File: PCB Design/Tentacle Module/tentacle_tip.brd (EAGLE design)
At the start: 45.7 x 15.2 mm, 8 parts, among them U2 ADXL345PATRICK

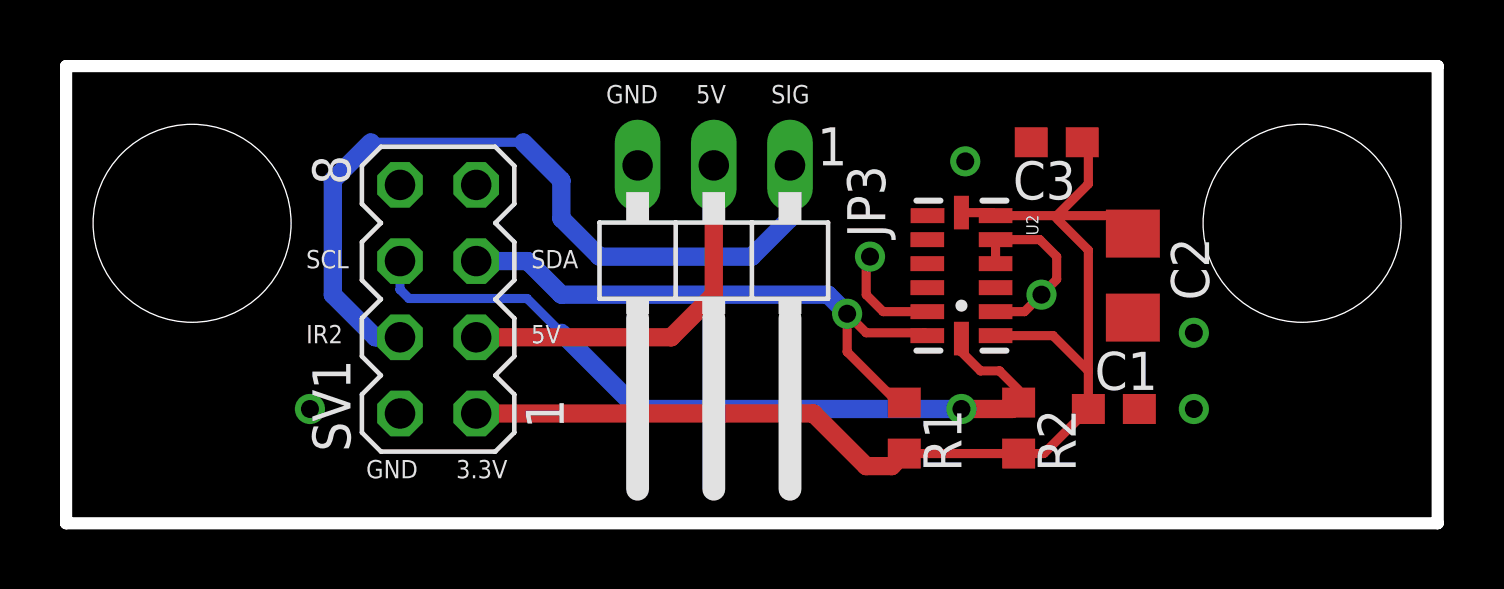
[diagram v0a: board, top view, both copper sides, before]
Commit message: Fixed up the  Tentacle tip board
routed the airwires that I forgot
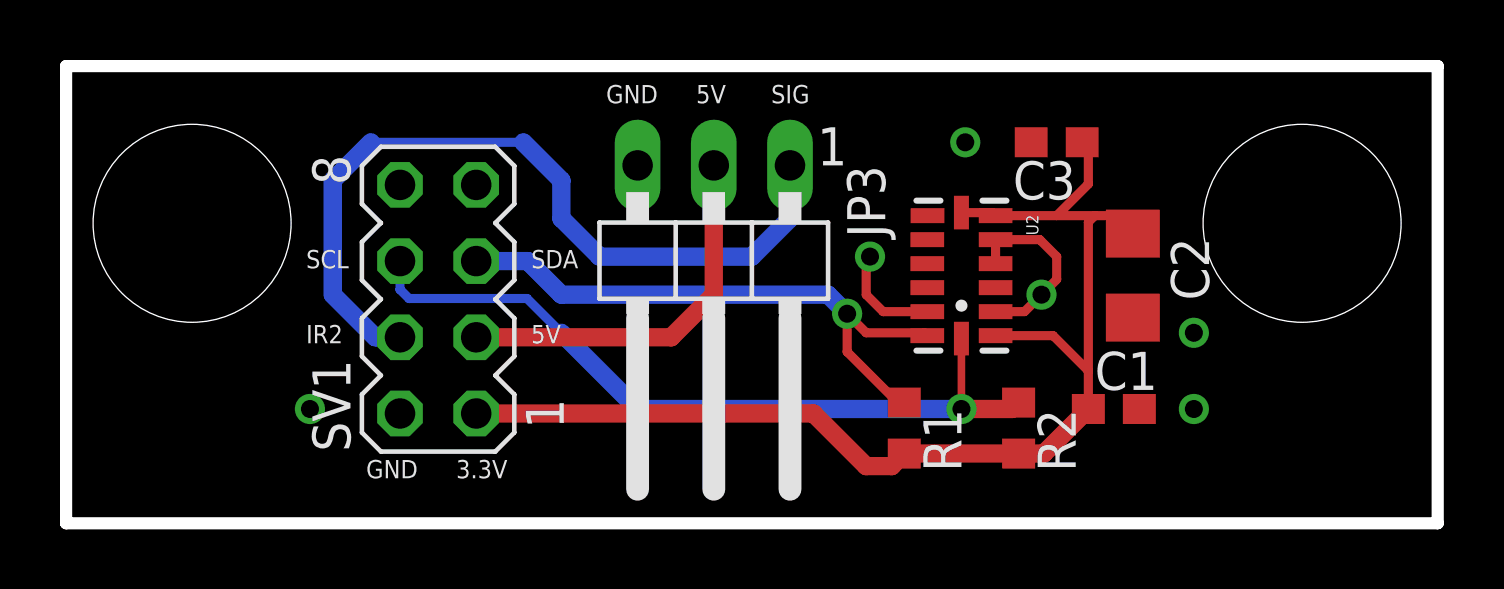
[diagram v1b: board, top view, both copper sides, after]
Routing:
- net +3.3V: track 41.3 -> 42.1 mm
- net SCL: track 26.2 -> 25.7 mm

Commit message: Modified labels and silkscreen
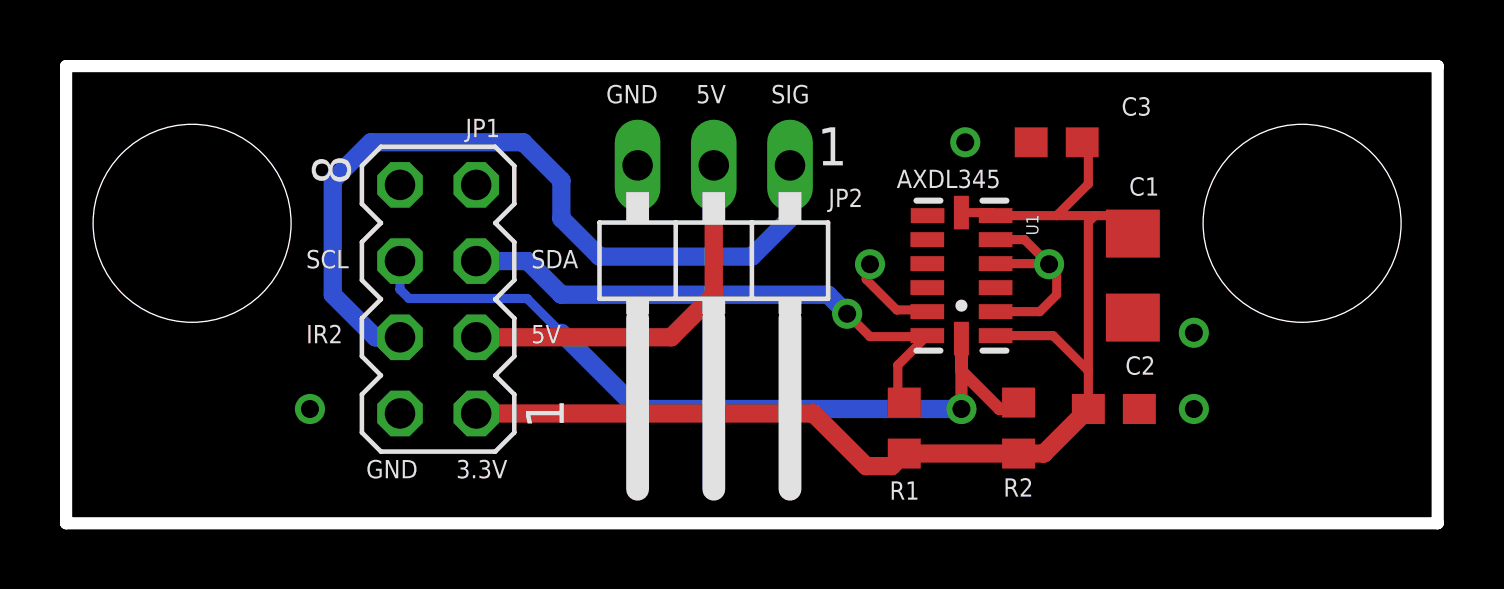
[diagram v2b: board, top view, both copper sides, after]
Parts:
- C1: value 0.1uF -> 10uF; device rcl:C0603 -> rcl:C1206
- C2: value 10uF -> 0.1uF; device rcl:C1206 -> rcl:C0603
- U1: value ADXL345PATRICK -> ADXL345
- moved C1 4.49 mm to (35.6, 8.26), turned to 270 degrees
- moved C2 4.49 mm to (34.9, 3.81), turned to 0 degrees
- renumbered JP3 to JP2, SV1 to JP1, U2 to U1
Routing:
- net SCL: track 25.7 -> 27.3 mm
- net SDA: track 19.9 -> 18.9 mm
- net GND: track 9.91 -> 10.6 mm
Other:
- board text added: "AXDL345"

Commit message: Modified Tentacle tip board to make pins longer
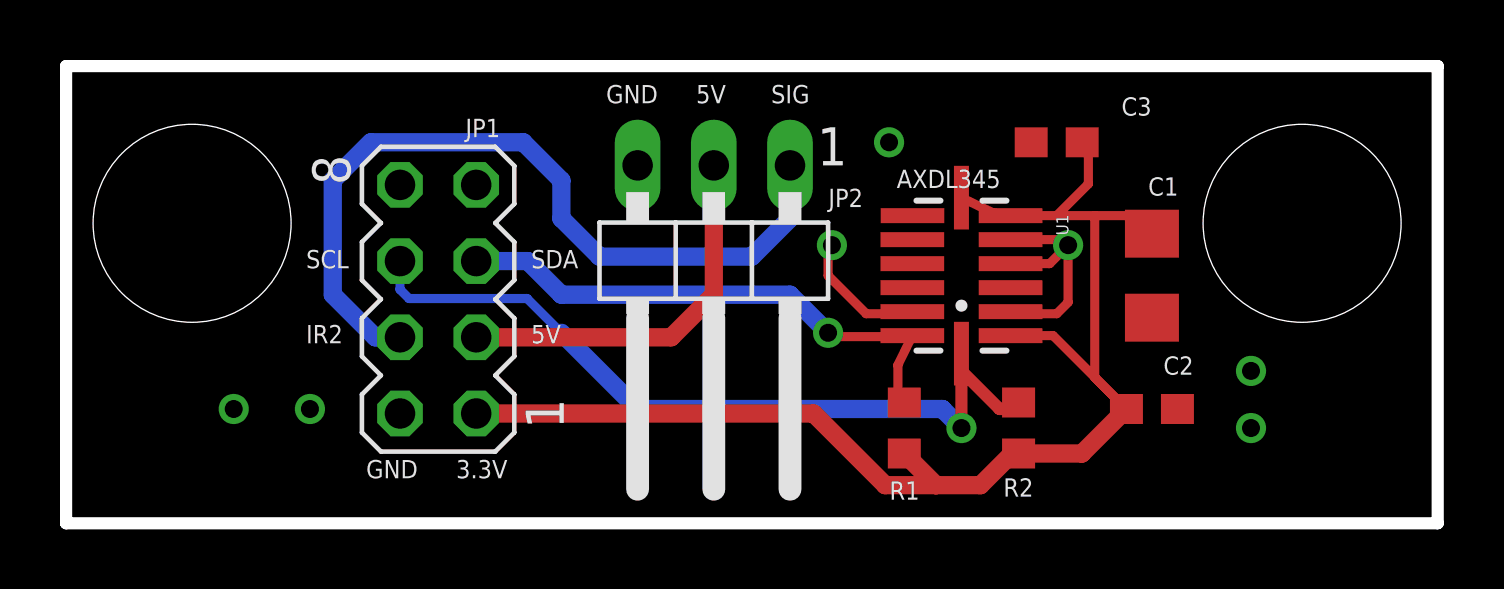
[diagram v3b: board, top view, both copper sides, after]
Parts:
- U1: device CBLA_Test_bed_Library:LGA14_1:1_PATRICK -> CBLA_Test_bed_Library:LGA14_LONG
- moved C2 1.27 mm to (36.2, 3.81)
- moved C1 0.63 mm to (36.2, 8.26)
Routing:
- net +3.3V: track 42.1 -> 46.6 mm
- net GND: track 10.6 -> 13.1 mm, vias 6 -> 7

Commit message: fixed the error with order of headers for IR sensor
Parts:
- renumbered JP1 to X1, JP2 to X2
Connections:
- net +5V: now also X2.3; no longer X2.2
- net GND: now also X2.2; no longer X2.3
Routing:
- net GND: track 13.1 -> 24.5 mm, vias 7 -> 8
- net +5V: track 12.8 -> 9.53 mm
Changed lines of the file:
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@@
 <setting verticaltext="up"/>
 </settings>
-<grid distance="0.05" unitdist="inch" unit="inch" style="lines" multiple="1" display="yes" altdistance="0.025" altunitdist="inch" altunit="inch"/>
+<grid distance="0.01" unitdist="inch" unit="inch" style="lines" multiple="1" display="yes" altdistance="0.005" altunitdist="inch" altunit="inch"/>
 <layers>
 <layer number="1" name="Top" color="4" fill="1" visible="yes" active="yes"/>
@@
 <hole x="4.2" y="10" drill="6.6"/>
 <hole x="41.2" y="10" drill="6.6"/>
-<text x="13" y="1.5" size="0.6096" layer="21">3.3V</text>
+<text x="15.54" y="2.135" size="0.6096" layer="21">3.3V</text>
 <text x="15.5" y="6" size="0.6096" layer="21">5V</text>
 <text x="15.5" y="8.5" size="0.6096" layer="21">SDA</text>
 <text x="8" y="8.5" size="0.6096" layer="21">SCL</text>
 <text x="8" y="6" size="0.6096" layer="21">IR2</text>
-<text x="10" y="1.5" size="0.6096" layer="21">GND</text>
+<text x="8.095" y="2.135" size="0.6096" layer="21">GND</text>
 <text x="23.5" y="14" size="0.6096" layer="21">SIG</text>
-<text x="21" y="14" size="0.6096" layer="21">5V</text>
-<text x="18" y="14" size="0.6096" layer="21">GND</text>
-<text x="27.686" y="11.176" size="0.6096" layer="21">AXDL345</text>
+<text x="18.46" y="14" size="0.6096" layer="21">5V</text>
+<text x="20.794" y="14" size="0.6096" layer="21">GND</text>
+<text x="26.924" y="6.096" size="0.6096" layer="21" rot="R90">AXDL345</text>
 </plain>
 <attributes>
@@
 <attribute name="VALUE" x="33.655" y="14.605" size="1.27" layer="27" rot="R180"/>
 </element>
-<element name="JP2" library="CBLA_Test_bed_Library" package="1X03/90" value="" x="21.59" y="8.12" smashed="yes" rot="R180">
+<element name="X2" library="CBLA_Test_bed_Library" package="1X03/90" value="" x="21.59" y="8.12" smashed="yes" rot="R180">
 <attribute name="NAME" x="25.408" y="10.541" size="0.6096" layer="25" ratio="10"/>
 <attribute name="VALUE" x="15.875" y="11.93" size="1.27" layer="27" rot="R270"/>
@@
 </element>
 <element name="U1" library="CBLA_Test_bed_Library" package="LGA14_LONG" value="ADXL345" x="29.845" y="8.255" rot="R270"/>
-<element name="JP1" library="CBLA_Test_bed_Library" package="MA04-2" value="" x="12.4" y="7.47" smashed="yes" rot="R90">
+<element name="X1" library="CBLA_Test_bed_Library" package="MA04-2" value="" x="12.4" y="7.47" smashed="yes" rot="R90">
 <attribute name="OC_NEWARK" value="unknown" x="12.4" y="7.47" size="1.778" layer="27" rot="R90" display="off"/>
 <attribute name="MPN" value="" x="12.4" y="7.47" size="1.778" layer="27" rot="R90" display="off"/>
@@
 <signals>
 <signal name="IR2">
-<contactref element="JP2" pad="1"/>
-<contactref element="JP1" pad="4"/>
+<contactref element="X2" pad="1"/>
+<contactref element="X1" pad="4"/>
 <wire x1="11.13" y1="6.2" x2="10.31" y2="6.2" width="0.6096" layer="16"/>
 <wire x1="10.31" y1="6.2" x2="8.89" y2="7.62" width="0.6096" layer="16"/>
@@
 </signal>
 <signal name="+5V">
-<contactref element="JP2" pad="2"/>
-<contactref element="JP1" pad="3"/>
-<wire x1="13.67" y1="6.2" x2="20.17" y2="6.2" width="0.6096" layer="1"/>
-<wire x1="20.17" y1="6.2" x2="21.59" y2="7.62" width="0.6096" layer="1"/>
-<wire x1="21.59" y1="7.62" x2="21.59" y2="11.93" width="0.6096" layer="1"/>
+<contactref element="X1" pad="3"/>
+<contactref element="X2" pad="3"/>
+<wire x1="13.67" y1="6.2" x2="16.36" y2="6.2" width="0.6096" layer="1"/>
+<wire x1="16.36" y1="6.2" x2="19.05" y2="8.89" width="0.6096" layer="1"/>
+<wire x1="19.05" y1="8.89" x2="19.05" y2="11.93" width="0.6096" layer="1"/>
 </signal>
 <signal name="+3.3V">
@@
 <contactref element="U1" pad="6"/>
 <contactref element="C3" pad="1"/>
-<contactref element="JP1" pad="1"/>
+<contactref element="X1" pad="1"/>
 <contactref element="U1" pad="7"/>
 <contactref element="R1" pad="2"/>
@@
 <contactref element="C2" pad="2"/>
 <contactref element="U1" pad="12"/>
-<contactref element="JP2" pad="3"/>
-<contactref element="JP1" pad="2"/>
+<contactref element="X1" pad="2"/>
 <via x="8.128" y="3.81" extent="1-16" drill="0.6"/>
 <via x="39.497" y="3.175" extent="1-16" drill="0.6"/>
@@
 <wire x1="26.67" y1="6.985" x2="28.1369" y2="6.985" width="0.3048" layer="1"/>
 <wire x1="28.1369" y1="6.985" x2="28.2069" y2="7.055" width="0.3048" layer="1"/>
+<contactref element="X2" pad="2"/>
+<wire x1="21.59" y1="5.715" x2="18.415" y2="5.715" width="0.6096" layer="1"/>
+<wire x1="18.415" y1="5.715" x2="17.78" y2="5.08" width="0.6096" layer="1"/>
+<wire x1="17.78" y1="5.08" x2="15.24" y2="5.08" width="0.6096" layer="1"/>
+<wire x1="15.367" y1="4.953" x2="12.319" y2="4.953" width="0.3048" layer="1"/>
+<wire x1="11.049" y1="3.683" x2="12.319" y2="4.953" width="0.3048" layer="1"/>
+<via x="15.748" y="4.953" extent="1-16" drill="0.6"/>
 </signal>
 <signal name="SCL">
-<contactref element="JP1" pad="6"/>
+<contactref element="X1" pad="6"/>
 <wire x1="11.13" y1="8.74" x2="11.13" y2="7.793" width="0.3048" layer="16"/>
 <wire x1="16.51" y1="6.35" x2="19.05" y2="3.81" width="0.6096" layer="16"/>
@@
 </signal>
 <signal name="SDA">
-<contactref element="JP1" pad="5"/>
+<contactref element="X1" pad="5"/>
 <wire x1="13.67" y1="8.74" x2="15.39" y2="8.74" width="0.6096" layer="16"/>
 <wire x1="15.39" y1="8.74" x2="16.51" y2="7.62" width="0.6096" layer="16"/>

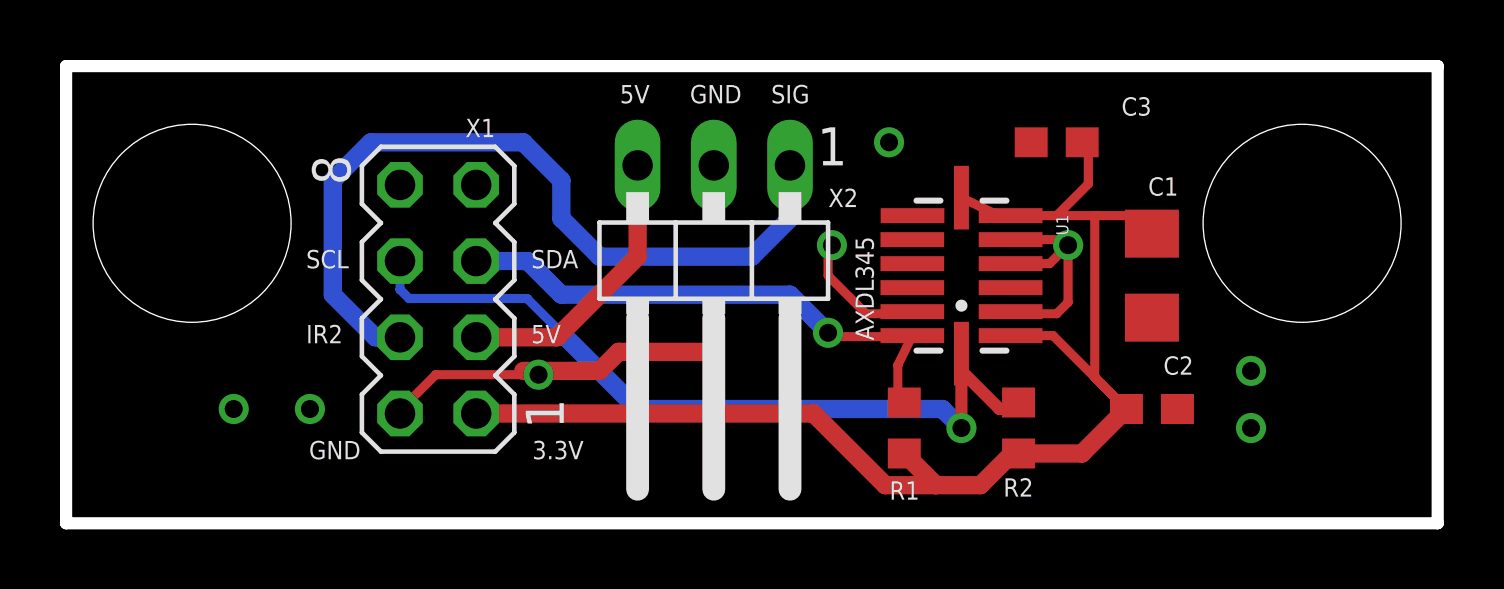
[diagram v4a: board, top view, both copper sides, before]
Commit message: Swapped the SDA and SCL pins on the Tentacle tip connector
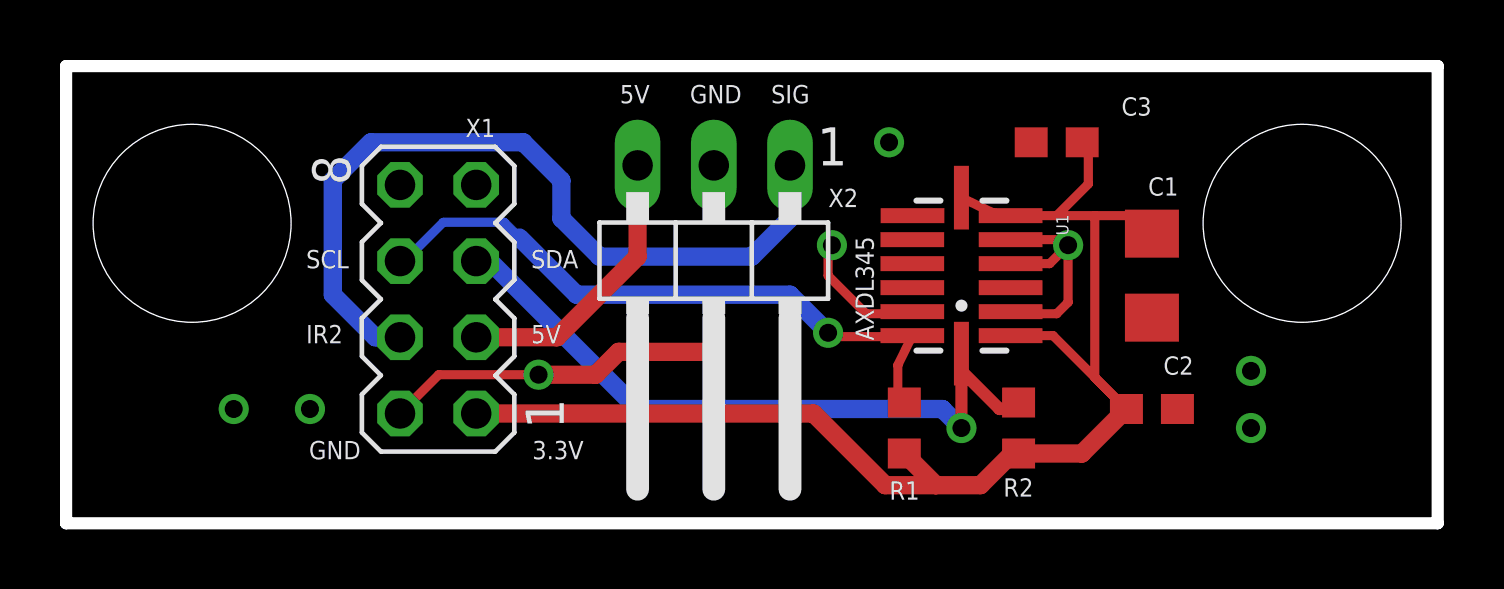
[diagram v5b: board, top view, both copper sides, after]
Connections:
- net SCL: now also X1.5; no longer X1.6
- net SDA: now also X1.6; no longer X1.5
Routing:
- net SDA: track 19.1 -> 22.7 mm
- net SCL: track 27.1 -> 24.1 mm
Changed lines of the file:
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@@
 <contactref element="X2" pad="2"/>
 <wire x1="21.59" y1="5.715" x2="18.415" y2="5.715" width="0.6096" layer="1"/>
-<wire x1="18.415" y1="5.715" x2="17.78" y2="5.08" width="0.6096" layer="1"/>
-<wire x1="17.78" y1="5.08" x2="15.24" y2="5.08" width="0.6096" layer="1"/>
-<wire x1="15.367" y1="4.953" x2="12.319" y2="4.953" width="0.3048" layer="1"/>
-<wire x1="11.049" y1="3.683" x2="12.319" y2="4.953" width="0.3048" layer="1"/>
+<wire x1="18.415" y1="5.715" x2="17.653" y2="4.953" width="0.6096" layer="1"/>
 <via x="15.748" y="4.953" extent="1-16" drill="0.6"/>
+<wire x1="17.653" y1="4.953" x2="15.748" y2="4.953" width="0.6096" layer="1"/>
+<wire x1="11.13" y1="3.66" x2="12.423" y2="4.953" width="0.3048" layer="1"/>
+<wire x1="12.423" y1="4.953" x2="15.748" y2="4.953" width="0.3048" layer="1"/>
 </signal>
 <signal name="SCL">
-<contactref element="X1" pad="6"/>
-<wire x1="11.13" y1="8.74" x2="11.13" y2="7.793" width="0.3048" layer="16"/>
-<wire x1="16.51" y1="6.35" x2="19.05" y2="3.81" width="0.6096" layer="16"/>
 <via x="29.845" y="3.175" extent="1-16" drill="0.6"/>
-<wire x1="11.13" y1="7.793" x2="11.43" y2="7.493" width="0.3048" layer="16"/>
-<wire x1="11.43" y1="7.493" x2="15.367" y2="7.493" width="0.3048" layer="16"/>
-<wire x1="15.367" y1="7.493" x2="16.51" y2="6.35" width="0.3048" layer="16"/>
 <contactref element="R2" pad="1"/>
 <contactref element="U1" pad="14"/>
@@
 <wire x1="19.05" y1="3.81" x2="29.21" y2="3.81" width="0.6096" layer="16"/>
 <wire x1="29.21" y1="3.81" x2="29.845" y2="3.175" width="0.6096" layer="16"/>
+<contactref element="X1" pad="5"/>
+<wire x1="19.05" y1="3.81" x2="14.12" y2="8.74" width="0.6096" layer="16"/>
+<wire x1="14.12" y1="8.74" x2="13.67" y2="8.74" width="0.6096" layer="16"/>
 </signal>
 <signal name="SDA">
-<contactref element="X1" pad="5"/>
-<wire x1="13.67" y1="8.74" x2="15.39" y2="8.74" width="0.6096" layer="16"/>
-<wire x1="15.39" y1="8.74" x2="16.51" y2="7.62" width="0.6096" layer="16"/>
-<wire x1="16.51" y1="7.62" x2="24.13" y2="7.62" width="0.6096" layer="16"/>
+<wire x1="17.018" y1="7.62" x2="24.13" y2="7.62" width="0.6096" layer="16"/>
 <via x="25.4" y="6.35" extent="1-16" drill="0.6"/>
 <contactref element="R1" pad="1"/>
@@
 <wire x1="25.527" y1="6.223" x2="25.4" y2="6.35" width="0.3048" layer="1"/>
 <wire x1="24.13" y1="7.62" x2="25.4" y2="6.35" width="0.6096" layer="16"/>
+<contactref element="X1" pad="6"/>
+<wire x1="17.018" y1="7.62" x2="15.113" y2="9.525" width="0.6096" layer="16"/>
+<wire x1="15.113" y1="9.525" x2="14.605" y2="10.033" width="0.3048" layer="16"/>
+<wire x1="14.605" y1="10.033" x2="12.573" y2="10.033" width="0.3048" layer="16"/>
+<wire x1="12.573" y1="10.033" x2="11.28" y2="8.74" width="0.3048" layer="16"/>
+<wire x1="11.28" y1="8.74" x2="11.13" y2="8.74" width="0.3048" layer="16"/>
 </signal>
 </signals>
